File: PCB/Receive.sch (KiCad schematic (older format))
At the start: 1 part

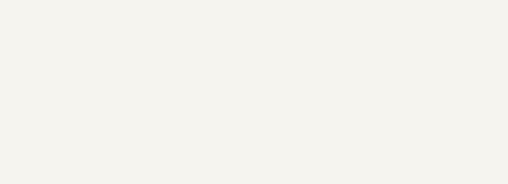
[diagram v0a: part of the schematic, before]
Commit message: Add diode pair to library
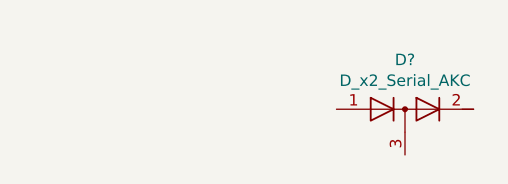
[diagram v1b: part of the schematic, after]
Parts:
- added D?: D_x2_Serial_AKC, Parts:MMBD7000L, symbol Device:D_x2_Serial_AKC
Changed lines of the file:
@@
 $Descr A4 11693 8268
 encoding utf-8
-Sheet 7 7
+Sheet 7 8
 Title ""
 Date ""
@@
 	1    0    0    -1
 $EndComp
+$Comp
+L Device:D_x2_Serial_AKC D?
+U 1 1 5DCEBFD1
+P 9450 3750
+F 0 "D?" H 9450 3966 50  0000 C CNN
+F 1 "D_x2_Serial_AKC" H 9450 3875 50  0000 C CNN
+F 2 "Parts:MMBD7000L" H 9450 3750 50  0001 C CNN
+F 3 "https://www.onsemi.com/products/discretes-drivers/diodes-rectifiers/small-signal-switching-diodes/mmbd7000l" H 9450 3750 50  0001 C CNN
+	1    9450 3750
+	1    0    0    -1
+$EndComp

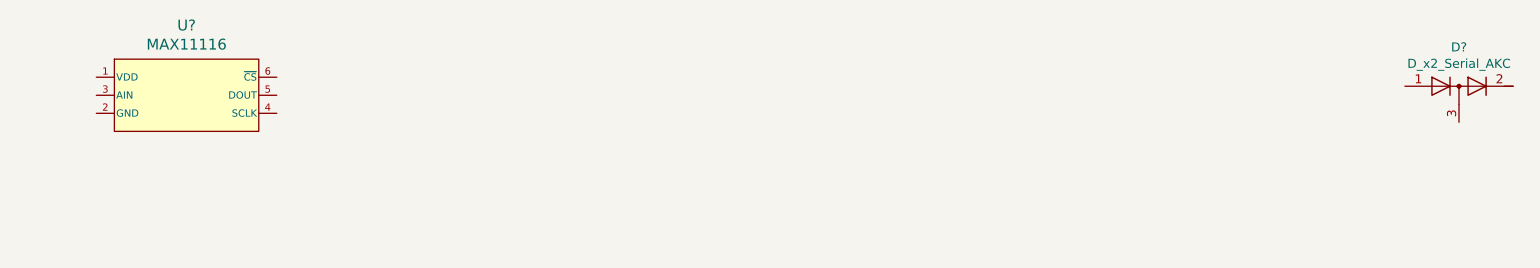
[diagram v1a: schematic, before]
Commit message: Added "near radio" warning to microcontroller pins, connected more ICs to power rails, added transducer capacitive coupling
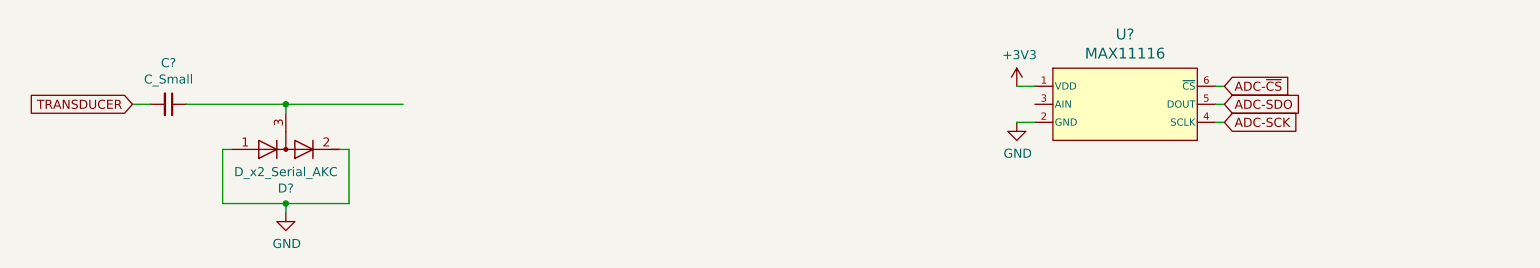
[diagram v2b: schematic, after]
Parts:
- added C?: C_Small, symbol Device:C_Small
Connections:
- net labels added: +3V3, ADC-SCK, ADC-SDO, ADC-~CS, GND, TRANSDUCER
- wire segments 0 -> 16
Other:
- moved on the sheet: D?, U?
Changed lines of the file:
@@
 L Parts:MAX11116 U?
 U 1 1 5DCE353E
-P 2400 3800
-F 0 "U?" H 2400 4187 60  0000 C CNN
-F 1 "MAX11116" H 2400 4081 60  0000 C CNN
-F 2 "Parts:SOT23" H 2400 3550 60  0001 C CNN
-F 3 "https://www.maximintegrated.com/en/products/analog/data-converters/analog-to-digital-converters/MAX11116.html" H 1900 3800 60  0001 C CNN
-	1    2400 3800
+P 7600 3850
+F 0 "U?" H 7600 4237 60  0000 C CNN
+F 1 "MAX11116" H 7600 4131 60  0000 C CNN
+F 2 "Parts:SOT23" H 7600 3600 60  0001 C CNN
+F 3 "https://www.maximintegrated.com/en/products/analog/data-converters/analog-to-digital-converters/MAX11116.html" H 7100 3850 60  0001 C CNN
+	1    7600 3850
 	1    0    0    -1
 $EndComp
@@
 L Device:D_x2_Serial_AKC D?
 U 1 1 5DCEBFD1
-P 9450 3750
-F 0 "D?" H 9450 3966 50  0000 C CNN
-F 1 "D_x2_Serial_AKC" H 9450 3875 50  0000 C CNN
-F 2 "Parts:MMBD7000L" H 9450 3750 50  0001 C CNN
-F 3 "https://www.onsemi.com/products/discretes-drivers/diodes-rectifiers/small-signal-switching-diodes/mmbd7000l" H 9450 3750 50  0001 C CNN
-	1    9450 3750
+P 2950 4100
+F 0 "D?" H 2950 4316 50  0000 C CNN
+F 1 "D_x2_Serial_AKC" H 2950 4225 50  0000 C CNN
+F 2 "Parts:MMBD7000L" H 2950 4100 50  0001 C CNN
+F 3 "https://www.onsemi.com/products/discretes-drivers/diodes-rectifiers/small-signal-switching-diodes/mmbd7000l" H 2950 4100 50  0001 C CNN
+	1    2950 4100
+	1    0    0    1
+$EndComp
+$Comp
+L power:+3V3 #PWR?
+U 1 1 5DE6A184
+P 7000 3750
+F 0 "#PWR?" H 7000 3600 50  0001 C CNN
+F 1 "+3V3" H 7015 3923 50  0000 C CNN
+F 2 "" H 7000 3750 50  0001 C CNN
+F 3 "" H 7000 3750 50  0001 C CNN
+	1    7000 3750
 	1    0    0    -1
 $EndComp
+$Comp
+L power:GND #PWR?
+U 1 1 5DE6B0BA
+P 7000 3950
+F 0 "#PWR?" H 7000 3700 50  0001 C CNN
+F 1 "GND" H 7005 3777 50  0000 C CNN
+F 2 "" H 7000 3950 50  0001 C CNN
+F 3 "" H 7000 3950 50  0001 C CNN
+	1    7000 3950
+	1    0    0    -1
+$EndComp
+Wire Wire Line
+	7000 3950 7100 3950
+Wire Wire Line
+	7000 3750 7100 3750
+Text GLabel 8150 3750 2    50   Input ~ 0
+ADC-~CS
+Text GLabel 8150 3950 2    50   Input ~ 0
+ADC-SCK
+Text GLabel 8150 3850 2    50   Input ~ 0
+ADC-SDO
+Wire Wire Line
+	8100 3750 8150 3750
+Wire Wire Line
+	8150 3850 8100 3850
+Wire Wire Line
+	8100 3950 8150 3950
+$Comp
+L power:GND #PWR?
+U 1 1 5DE74334
+P 2950 4450
+F 0 "#PWR?" H 2950 4200 50  0001 C CNN
+F 1 "GND" H 2955 4277 50  0000 C CNN
+F 2 "" H 2950 4450 50  0001 C CNN
+F 3 "" H 2950 4450 50  0001 C CNN
+	1    2950 4450
+	1    0    0    -1
+$EndComp
+Wire Wire Line
+	2600 4400 2950 4400
+Wire Wire Line
+	3300 4400 2950 4400
+Connection ~ 2950 4400
+Wire Wire Line
+	2950 4450 2950 4400
+Wire Wire Line
+	3300 4400 3300 4100
+Wire Wire Line
+	3300 4100 3250 4100
+Wire Wire Line
+	2650 4100 2600 4100
+Wire Wire Line
+	2600 4100 2600 4400
+$Comp
+L Device:C_Small C?
+U 1 1 5DE7BD62
+P 2300 3850
+F 0 "C?" V 2071 3850 50  0000 C CNN
+F 1 "C_Small" V 2162 3850 50  0000 C CNN
+F 2 "" H 2300 3850 50  0001 C CNN
+F 3 "~" H 2300 3850 50  0001 C CNN
+	1    2300 3850
+	0    1    1    0
+$EndComp
+Wire Wire Line
+	2950 3850 2950 3900
+Wire Wire Line
+	2400 3850 2950 3850
+Wire Wire Line
+	2950 3850 3600 3850
+Connection ~ 2950 3850
+Text GLabel 2100 3850 0    50   Input ~ 0
+TRANSDUCER
+Wire Wire Line
+	2100 3850 2200 3850
 $EndSCHEMATC

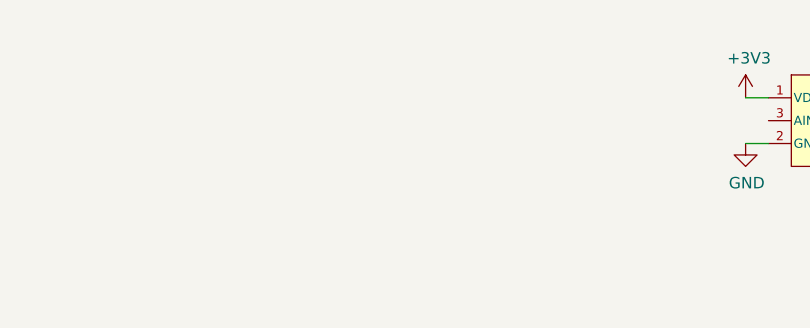
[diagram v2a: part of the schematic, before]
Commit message: Added low-noise supply rails, changed 100nF capacitors to 0603 footprint, fixed ENS210 footprint, added decoupling capacitors to microcontroller
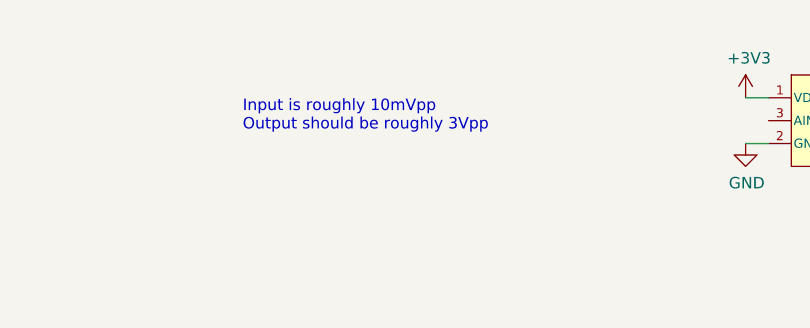
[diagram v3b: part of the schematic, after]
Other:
- note added: "Input is roughly 10mVpp\nOutput should be roughly 3Vpp"
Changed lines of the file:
@@
 Wire Wire Line
 	2100 3850 2200 3850
+Text Notes 4800 3900 0    50   ~ 0
+Input is roughly 10mVpp\nOutput should be roughly 3Vpp
 $EndSCHEMATC

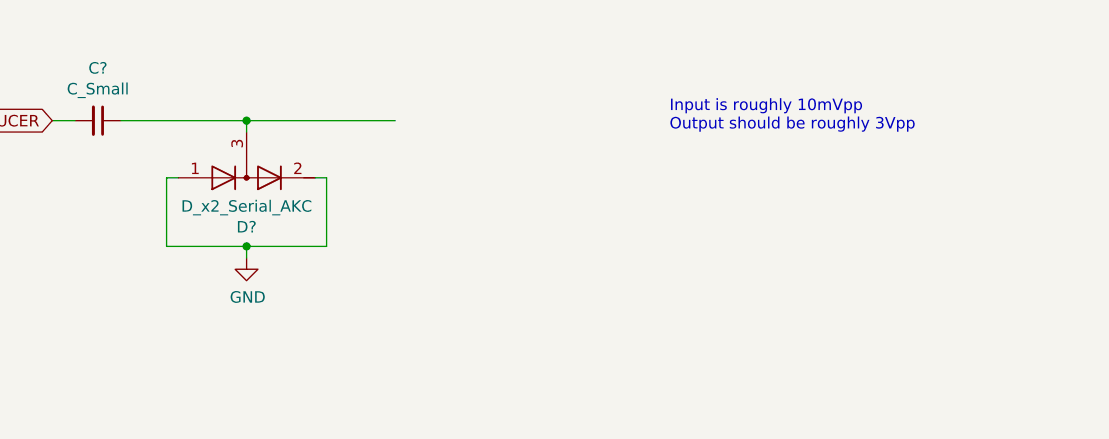
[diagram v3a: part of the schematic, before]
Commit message: Switch to diodes that will waste less transmit power, add amplifier to generate transmit midrail, add enable signal to final amplifier
Enable signal to final amplifier is important, as it will allow us to conserve power when not transmitting. This should help keep the amplifier from overheating.
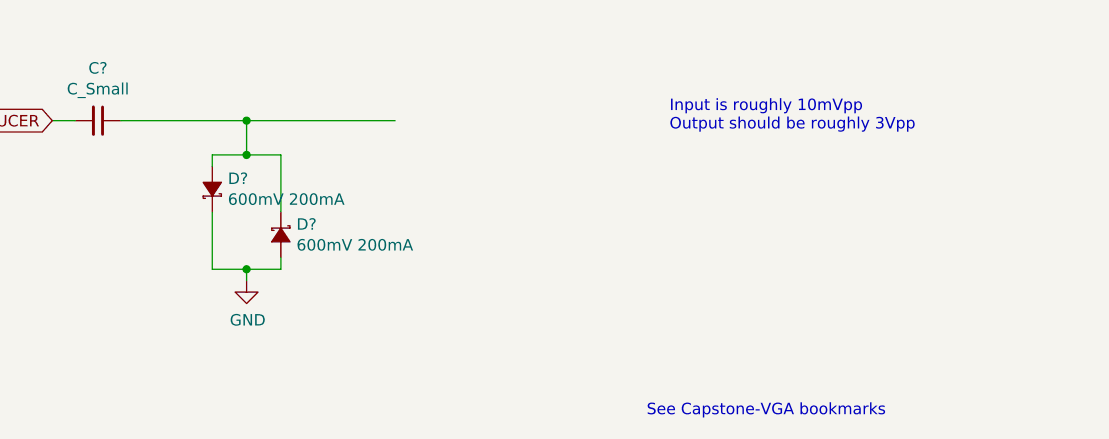
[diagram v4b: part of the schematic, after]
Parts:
- removed D?: D_x2_Serial_AKC, Parts:MMBD7000L, symbol Device:D_x2_Serial_AKC
- added D? (x2): 600mV 200mA, Diodes_SMD:D_SOD-523, symbol Device:D_Schottky_Small_ALT
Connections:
- wire segments 16 -> 18
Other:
- note added: "See Capstone-VGA bookmarks"
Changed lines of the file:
@@
-$EndComp
-$Comp
-L Device:D_x2_Serial_AKC D?
-U 1 1 5DCEBFD1
-P 2950 4100
-F 0 "D?" H 2950 4316 50  0000 C CNN
-F 1 "D_x2_Serial_AKC" H 2950 4225 50  0000 C CNN
-F 2 "Parts:MMBD7000L" H 2950 4100 50  0001 C CNN
-F 3 "https://www.onsemi.com/products/discretes-drivers/diodes-rectifiers/small-signal-switching-diodes/mmbd7000l" H 2950 4100 50  0001 C CNN
-	1    2950 4100
-	1    0    0    1
 $EndComp
 $Comp
@@
 L power:GND #PWR?
 U 1 1 5DE74334
-P 2950 4450
-F 0 "#PWR?" H 2950 4200 50  0001 C CNN
-F 1 "GND" H 2955 4277 50  0000 C CNN
-F 2 "" H 2950 4450 50  0001 C CNN
-F 3 "" H 2950 4450 50  0001 C CNN
-	1    2950 4450
+P 2950 4550
+F 0 "#PWR?" H 2950 4300 50  0001 C CNN
+F 1 "GND" H 2955 4377 50  0000 C CNN
+F 2 "" H 2950 4550 50  0001 C CNN
+F 3 "" H 2950 4550 50  0001 C CNN
+	1    2950 4550
 	1    0    0    -1
 $EndComp
-Wire Wire Line
-	2600 4400 2950 4400
-Wire Wire Line
-	3300 4400 2950 4400
-Connection ~ 2950 4400
-Wire Wire Line
-	2950 4450 2950 4400
-Wire Wire Line
-	3300 4400 3300 4100
-Wire Wire Line
-	3300 4100 3250 4100
-Wire Wire Line
-	2650 4100 2600 4100
-Wire Wire Line
-	2600 4100 2600 4400
 $Comp
 L Device:C_Small C?
@@
 $EndComp
 Wire Wire Line
-	2950 3850 2950 3900
-Wire Wire Line
 	2400 3850 2950 3850
 Wire Wire Line
@@
 Text Notes 4800 3900 0    50   ~ 0
 Input is roughly 10mVpp\nOutput should be roughly 3Vpp
+Text Notes 4700 5150 0    50   ~ 0
+See Capstone-VGA bookmarks
+$Comp
+L Device:D_Schottky_Small_ALT D?
+U 1 1 5DF00EE8
+P 3100 4350
+F 0 "D?" V 3054 4418 50  0000 L CNN
+F 1 "600mV 200mA" V 3145 4418 50  0000 L CNN
+F 2 "Diodes_SMD:D_SOD-523" V 3100 4350 50  0001 C CNN
+F 3 "https://www.digikey.ca/product-detail/en/on-semiconductor/RB520S30T5G/RB520S30T5GOSCT-ND/5213385" V 3100 4350 50  0001 C CNN
+	1    3100 4350
+	0    1    1    0
+$EndComp
+$Comp
+L Device:D_Schottky_Small_ALT D?
+U 1 1 5DF02261
+P 2800 4150
+F 0 "D?" V 2846 4082 50  0000 R CNN
+F 1 "600mV 200mA" V 2755 4082 50  0000 R CNN
+F 2 "Diodes_SMD:D_SOD-523" V 2800 4150 50  0001 C CNN
+F 3 "https://www.digikey.ca/product-detail/en/on-semiconductor/RB520S30T5G/RB520S30T5GOSCT-ND/5213385" V 2800 4150 50  0001 C CNN
+	1    2800 4150
+	0    -1   -1   0
+$EndComp
+Wire Wire Line
+	2800 4050 2800 4000
+Wire Wire Line
+	2800 4000 2950 4000
+Wire Wire Line
+	3100 4000 3100 4250
+Wire Wire Line
+	2950 3850 2950 4000
+Connection ~ 2950 4000
+Wire Wire Line
+	2950 4000 3100 4000
+Wire Wire Line
+	2800 4250 2800 4500
+Wire Wire Line
+	2800 4500 2950 4500
+Wire Wire Line
+	3100 4500 3100 4450
+Wire Wire Line
+	2950 4500 2950 4550
+Connection ~ 2950 4500
+Wire Wire Line
+	2950 4500 3100 4500
 $EndSCHEMATC

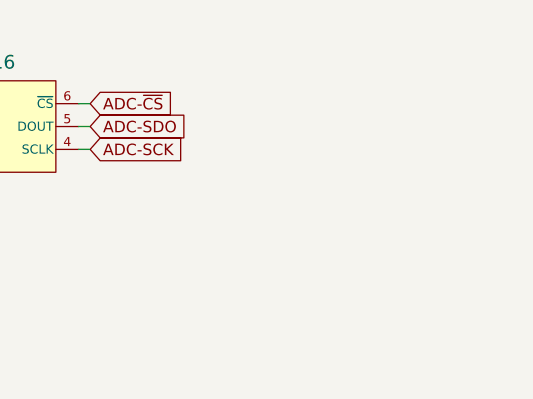
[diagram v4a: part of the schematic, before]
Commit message: Add decoupling capacitors for components without
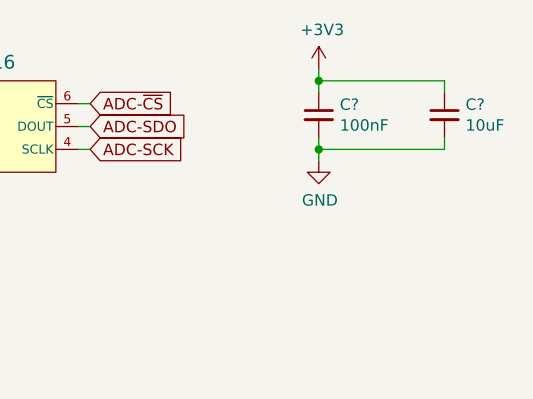
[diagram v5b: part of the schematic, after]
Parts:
- added C?: 10uF, Capacitors_SMD:C_0805_HandSoldering, symbol Device:C_Small
- added C?: 100nF, Capacitors_SMD:C_0603_HandSoldering, symbol Device:C_Small
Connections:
- wire segments 18 -> 26
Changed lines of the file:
@@
 Wire Wire Line
 	2950 4500 3100 4500
+$Comp
+L Device:C_Small C?
+U 1 1 5E3D409D
+P 9700 3800
+F 0 "C?" H 9792 3846 50  0000 L CNN
+F 1 "10uF" H 9792 3755 50  0000 L CNN
+F 2 "Capacitors_SMD:C_0805_HandSoldering" H 9700 3800 50  0001 C CNN
+F 3 "https://www.digikey.ca/product-detail/en/kemet/C0805C106K8PACTU/399-4925-1-ND/1090920" H 9700 3800 50  0001 C CNN
+	1    9700 3800
+	1    0    0    -1
+$EndComp
+$Comp
+L power:+3V3 #PWR?
+U 1 1 5E3D46BE
+P 9150 3600
+F 0 "#PWR?" H 9150 3450 50  0001 C CNN
+F 1 "+3V3" H 9165 3773 50  0000 C CNN
+F 2 "" H 9150 3600 50  0001 C CNN
+F 3 "" H 9150 3600 50  0001 C CNN
+	1    9150 3600
+	1    0    0    -1
+$EndComp
+$Comp
+L power:GND #PWR?
+U 1 1 5E3D4BAC
+P 9150 4000
+F 0 "#PWR?" H 9150 3750 50  0001 C CNN
+F 1 "GND" H 9155 3827 50  0000 C CNN
+F 2 "" H 9150 4000 50  0001 C CNN
+F 3 "" H 9150 4000 50  0001 C CNN
+	1    9150 4000
+	1    0    0    -1
+$EndComp
+$Comp
+L Device:C_Small C?
+U 1 1 5E3D52F8
+P 9150 3800
+F 0 "C?" H 9242 3846 50  0000 L CNN
+F 1 "100nF" H 9242 3755 50  0000 L CNN
+F 2 "Capacitors_SMD:C_0603_HandSoldering" H 9150 3800 50  0001 C CNN
+F 3 "https://www.digikey.ca/product-detail/en/w-rth-elektronik/885012206020/732-7939-1-ND/5454566" H 9150 3800 50  0001 C CNN
+	1    9150 3800
+	1    0    0    -1
+$EndComp
+Wire Wire Line
+	9150 3600 9150 3650
+Wire Wire Line
+	9150 3650 9700 3650
+Wire Wire Line
+	9700 3650 9700 3700
+Connection ~ 9150 3650
+Wire Wire Line
+	9150 3650 9150 3700
+Wire Wire Line
+	9700 3900 9700 3950
+Wire Wire Line
+	9700 3950 9150 3950
+Wire Wire Line
+	9150 3950 9150 3900
+Wire Wire Line
+	9150 3950 9150 4000
+Connection ~ 9150 3950
 $EndSCHEMATC

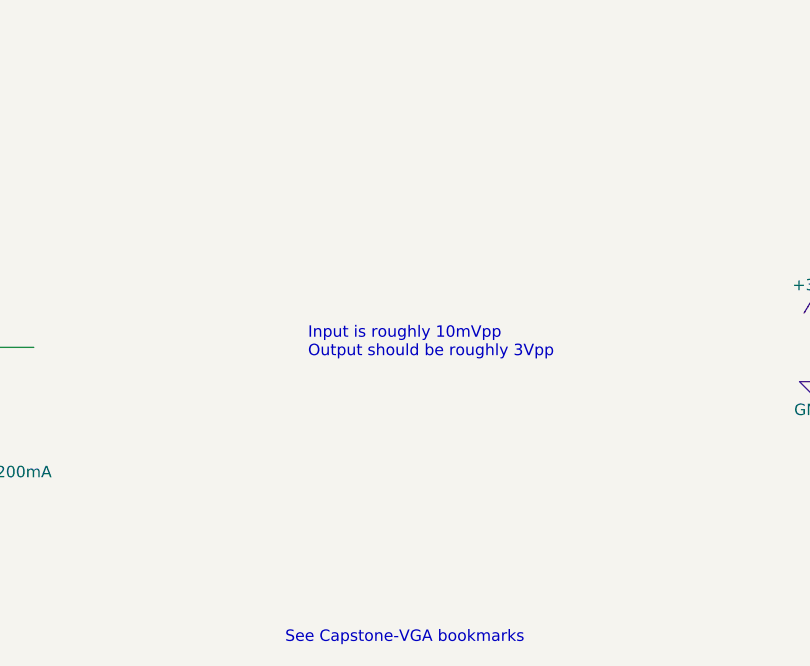
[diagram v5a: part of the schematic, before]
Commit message: Prepare for receive opamps
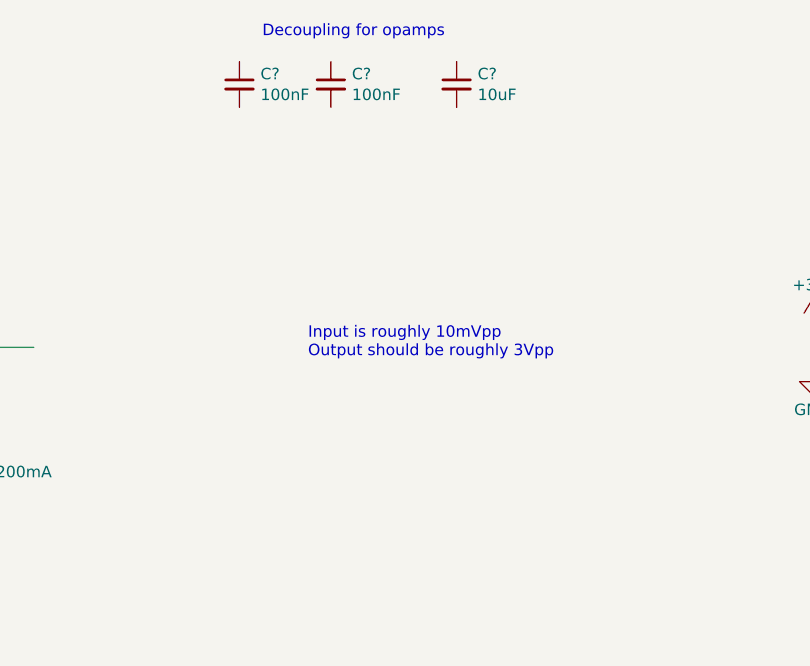
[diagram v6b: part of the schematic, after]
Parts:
- added C? (x2): 100nF, Capacitors_SMD:C_0603_HandSoldering, symbol Device:C_Small
- added C?: 10uF, Capacitors_SMD:C_0805_HandSoldering, symbol Device:C_Small
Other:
- note added: "Decoupling for opamps"
- note removed: "See Capstone-VGA bookmarks"
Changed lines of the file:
@@
 Text Notes 4800 3900 0    50   ~ 0
 Input is roughly 10mVpp\nOutput should be roughly 3Vpp
-Text Notes 4700 5150 0    50   ~ 0
-See Capstone-VGA bookmarks
 $Comp
 L Device:D_Schottky_Small_ALT D?
@@
 	9150 3950 9150 4000
 Connection ~ 9150 3950
+$Comp
+L Device:C_Small C?
+U 1 1 5E132FDE
+P 4500 2700
+F 0 "C?" H 4592 2746 50  0000 L CNN
+F 1 "100nF" H 4592 2655 50  0000 L CNN
+F 2 "Capacitors_SMD:C_0603_HandSoldering" H 4500 2700 50  0001 C CNN
+F 3 "https://www.digikey.ca/product-detail/en/w-rth-elektronik/885012206020/732-7939-1-ND/5454566" H 4500 2700 50  0001 C CNN
+	1    4500 2700
+	1    0    0    -1
+$EndComp
+$Comp
+L Device:C_Small C?
+U 1 1 5E133797
+P 4900 2700
+F 0 "C?" H 4992 2746 50  0000 L CNN
+F 1 "100nF" H 4992 2655 50  0000 L CNN
+F 2 "Capacitors_SMD:C_0603_HandSoldering" H 4900 2700 50  0001 C CNN
+F 3 "https://www.digikey.ca/product-detail/en/w-rth-elektronik/885012206020/732-7939-1-ND/5454566" H 4900 2700 50  0001 C CNN
+	1    4900 2700
+	1    0    0    -1
+$EndComp
+$Comp
+L Device:C_Small C?
+U 1 1 5E133C95
+P 5450 2700
+F 0 "C?" H 5542 2746 50  0000 L CNN
+F 1 "10uF" H 5542 2655 50  0000 L CNN
+F 2 "Capacitors_SMD:C_0805_HandSoldering" H 5450 2700 50  0001 C CNN
+F 3 "https://www.digikey.ca/product-detail/en/kemet/C0805C106K8PACTU/399-4925-1-ND/1090920" H 5450 2700 50  0001 C CNN
+	1    5450 2700
+	1    0    0    -1
+$EndComp
+Text Notes 4600 2500 0    50   ~ 0
+Decoupling for opamps
 $EndSCHEMATC
